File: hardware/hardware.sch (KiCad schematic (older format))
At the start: 12 parts, among them P1 CONN_01X08, P2 CONN_01X08, P3 CONN_01X02, P4 CONN_01X03

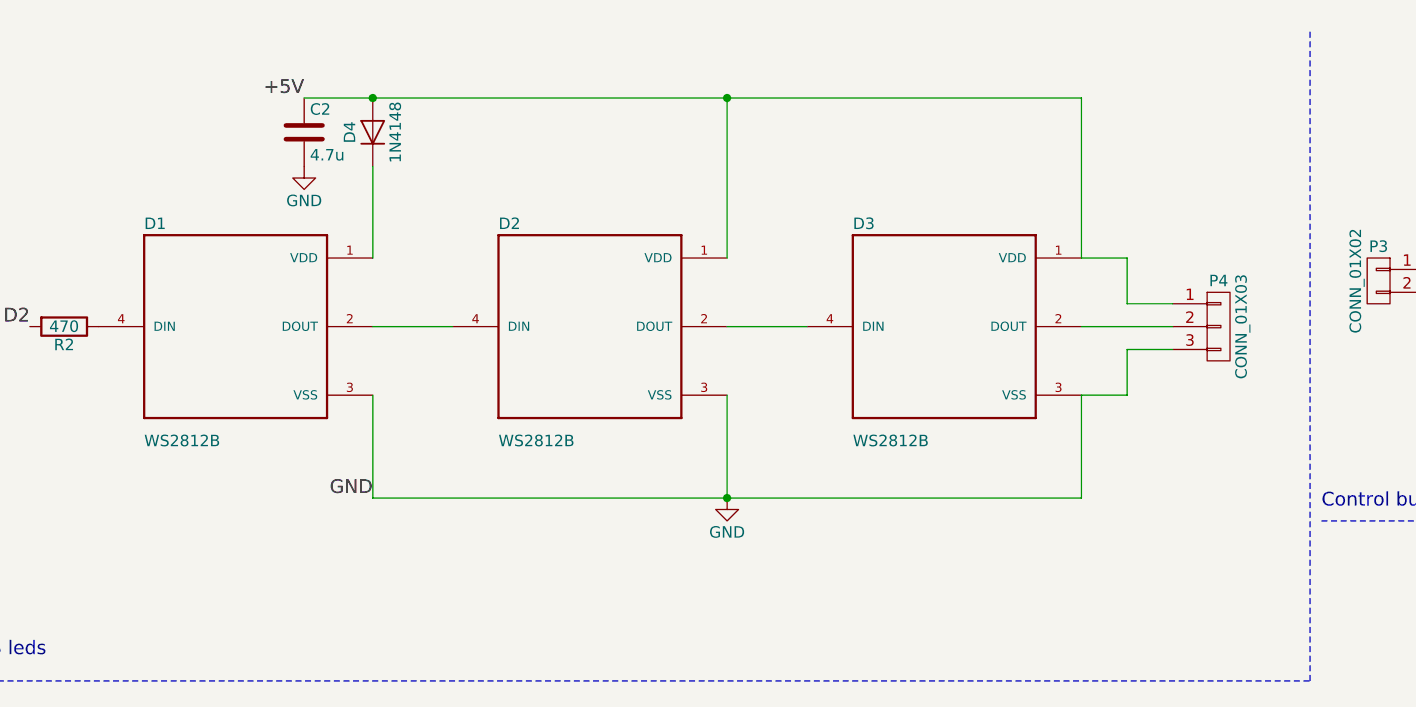
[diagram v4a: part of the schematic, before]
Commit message: v3.1, refactoring for only one Neopixel
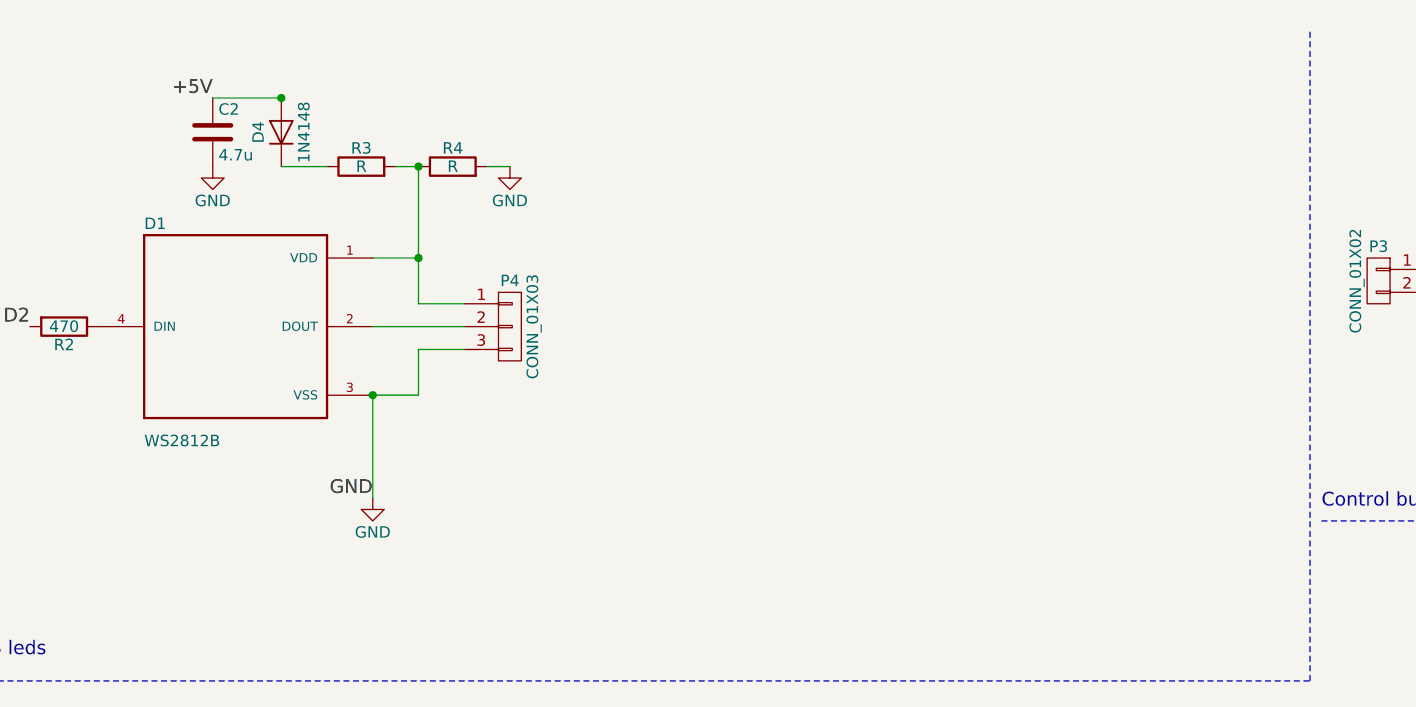
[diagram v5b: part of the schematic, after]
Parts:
- removed D2, D3: WS2812B, WS2812B:LED_WS2812B, symbol WS2812B
- added R3, R4: R, Resistors_THT:R_Axial_DIN0204_L3.6mm_D1.6mm_P2.54mm_Vertical, symbol R
- C1, C2: footprint Capacitors_SMD:C_0402 -> Capacitors_THT:C_Disc_D3.8mm_W2.6mm_P2.50mm
- D4: footprint Diodes_SMD:MiniMELF_Standard -> Diodes_THT:D_DO-15_P2.54mm_Vertical_KathodeUp
- P3: footprint Connect:PINHEAD1-2 -> Pin_Headers:Pin_Header_Angled_1x02
- P4: footprint Connect:PINHEAD1-3 -> Pin_Headers:Pin_Header_Angled_1x03
- R1, R2: footprint Resistors_SMD:R_0402 -> Resistors_THT:R_Axial_DIN0204_L3.6mm_D1.6mm_P2.54mm_Vertical
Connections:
- net +5V: no longer P4.1 (P1)
- net GND: now also R4.2
- net at D1.1 (VDD): now also P4.1 (P1), R3.2, R4.1; no longer D4.1 (K)
- net at D1.2 (DOUT): now also P4.2 (P2)
- new net: D4.1 (K), R3.1
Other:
- moved on the sheet: C2, D4, P4
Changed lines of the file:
@@
 encoding utf-8
 Sheet 1 1
-Title "SweetTime"
-Date "2016-06-27"
-Rev "2.0"
-Comp "Galilabs"
-Comment1 "Fablab Lannion"
-Comment2 "http://u.dinask.eu/trender"
+Title "Trender Led Shield"
+Date "2018-02-18"
+Rev "3.1"
+Comp "Fablab de Lannion"
+Comment1 "http://u.dinask.eu/trender"
+Comment2 "Trender project"
 Comment3 ""
 Comment4 ""
@@
 $EndComp
 $Comp
-L WS2812B D2
-U 1 1 577174D3
-P 3300 1800
-F 0 "D2" H 2900 2250 50  0000 L CNN
-F 1 "WS2812B" H 2900 1300 50  0000 L CNN
-F 2 "WS2812B:LED_WS2812B" H 3300 1800 50  0001 L CNN
-F 3 "" H 3300 1800 60  0000 C CNN
-	1    3300 1800
-	1    0    0    -1
-$EndComp
-$Comp
-L WS2812B D3
-U 1 1 57717547
-P 4850 1800
-F 0 "D3" H 4450 2250 50  0000 L CNN
-F 1 "WS2812B" H 4450 1300 50  0000 L CNN
-F 2 "WS2812B:LED_WS2812B" H 4850 1800 50  0001 L CNN
-F 3 "" H 4850 1800 60  0000 C CNN
-	1    4850 1800
-	1    0    0    -1
-$EndComp
-Wire Wire Line
-	3900 1800 4250 1800
-Wire Wire Line
-	2350 1800 2700 1800
-$Comp
 L D D4
 U 1 1 57717974
-P 2350 950
-F 0 "D4" H 2350 1050 50  0000 C CNN
-F 1 "1N4148" H 2350 850 50  0000 C CNN
-F 2 "Diodes_SMD:MiniMELF_Standard" H 2350 950 60  0001 C CNN
-F 3 "" H 2350 950 60  0000 C CNN
-	1    2350 950
+P 1950 950
+F 0 "D4" H 1950 1050 50  0000 C CNN
+F 1 "1N4148" H 1950 850 50  0000 C CNN
+F 2 "Diodes_THT:D_DO-15_P2.54mm_Vertical_KathodeUp" H 1950 950 60  0001 C CNN
+F 3 "" H 1950 950 60  0000 C CNN
+	1    1950 950
 	0    -1   -1   0
 $EndComp
 Wire Wire Line
-	2350 1500 2350 1100
-Wire Wire Line
-	2050 800  5450 800
-Wire Wire Line
-	3900 800  3900 1500
-Wire Wire Line
-	5450 800  5450 1500
-Connection ~ 3900 800
-Text Label 2050 800  2    60   ~ 0
+	1650 800  1950 800
+Text Label 1650 800  2    60   ~ 0
 +5V
 Wire Wire Line
 	2350 2100 2350 2550
-Wire Wire Line
-	2350 2550 5450 2550
-Wire Wire Line
-	3900 2550 3900 2100
-Wire Wire Line
-	5450 2550 5450 2100
-Connection ~ 3900 2550
 Text Label 2350 2550 2    60   ~ 0
 GND
@@
 F 0 "R1" V 7380 1000 50  0000 C CNN
 F 1 "10K" V 7300 1000 50  0000 C CNN
-F 2 "Resistors_SMD:R_0402" V 7230 1000 30  0001 C CNN
+F 2 "Resistors_THT:R_Axial_DIN0204_L3.6mm_D1.6mm_P2.54mm_Vertical" V 7230 1000 30  0001 C CNN
 F 3 "" H 7300 1000 30  0000 C CNN
 	1    7300 1000
@@
 F 0 "C1" H 7325 1650 50  0000 L CNN
 F 1 "10n" H 7325 1450 50  0000 L CNN
-F 2 "Capacitors_SMD:C_0402" H 7338 1400 30  0001 C CNN
+F 2 "Capacitors_THT:C_Disc_D3.8mm_W2.6mm_P2.50mm" H 7338 1400 30  0001 C CNN
 F 3 "" H 7300 1550 60  0000 C CNN
 	1    7300 1550
@@
 L GND #PWR06
 U 1 1 5771848D
-P 3900 2550
-F 0 "#PWR06" H 3900 2300 50  0001 C CNN
-F 1 "GND" H 3900 2400 50  0000 C CNN
-F 2 "" H 3900 2550 60  0000 C CNN
-F 3 "" H 3900 2550 60  0000 C CNN
-	1    3900 2550
+P 2350 2550
+F 0 "#PWR06" H 2350 2300 50  0001 C CNN
+F 1 "GND" H 2350 2400 50  0000 C CNN
+F 2 "" H 2350 2550 60  0000 C CNN
+F 3 "" H 2350 2550 60  0000 C CNN
+	1    2350 2550
 	1    0    0    -1
 $EndComp
@@
 F 0 "P3" H 6750 1750 50  0000 C CNN
 F 1 "CONN_01X02" V 6850 1600 50  0000 C CNN
-F 2 "Connect:PINHEAD1-2" H 6750 1600 60  0001 C CNN
+F 2 "Pin_Headers:Pin_Header_Angled_1x02" H 6750 1600 60  0001 C CNN
 F 3 "" H 6750 1600 60  0000 C CNN
 	1    6750 1600
@@
 F 0 "R2" V 1080 1800 50  0000 C CNN
 F 1 "470" V 1000 1800 50  0000 C CNN
-F 2 "Resistors_SMD:R_0402" V 930 1800 30  0001 C CNN
+F 2 "Resistors_THT:R_Axial_DIN0204_L3.6mm_D1.6mm_P2.54mm_Vertical" V 930 1800 30  0001 C CNN
 F 3 "" H 1000 1800 30  0000 C CNN
 	1    1000 1800
@@
 L C C2
 U 1 1 5772A7DC
-P 2050 950
-F 0 "C2" H 2075 1050 50  0000 L CNN
-F 1 "4.7u" H 2075 850 50  0000 L CNN
-F 2 "Capacitors_SMD:C_0402" H 2088 800 30  0001 C CNN
-F 3 "" H 2050 950 60  0000 C CNN
-	1    2050 950
-	1    0    0    -1
-$EndComp
-Connection ~ 2350 800
+P 1650 950
+F 0 "C2" H 1675 1050 50  0000 L CNN
+F 1 "4.7u" H 1675 850 50  0000 L CNN
+F 2 "Capacitors_THT:C_Disc_D3.8mm_W2.6mm_P2.50mm" H 1688 800 30  0001 C CNN
+F 3 "" H 1650 950 60  0000 C CNN
+	1    1650 950
+	1    0    0    -1
+$EndComp
+Connection ~ 1950 800
 $Comp
 L GND #PWR07
 U 1 1 5772A872
-P 2050 1100
-F 0 "#PWR07" H 2050 850 50  0001 C CNN
-F 1 "GND" H 2050 950 50  0000 C CNN
-F 2 "" H 2050 1100 60  0000 C CNN
-F 3 "" H 2050 1100 60  0000 C CNN
-	1    2050 1100
+P 1650 1100
+F 0 "#PWR07" H 1650 850 50  0001 C CNN
+F 1 "GND" H 1650 950 50  0000 C CNN
+F 2 "" H 1650 1100 60  0000 C CNN
+F 3 "" H 1650 1100 60  0000 C CNN
+	1    1650 1100
 	1    0    0    -1
 $EndComp
@@
 L CONN_01X03 P4
 U 1 1 5772F386
-P 6050 1800
-F 0 "P4" H 6050 2000 50  0000 C CNN
-F 1 "CONN_01X03" V 6150 1800 50  0000 C CNN
-F 2 "Connect:PINHEAD1-3" H 6050 1800 60  0001 C CNN
-F 3 "" H 6050 1800 60  0000 C CNN
-	1    6050 1800
-	1    0    0    -1
-$EndComp
-Wire Wire Line
-	5450 1500 5650 1500
-Wire Wire Line
-	5650 1500 5650 1700
-Wire Wire Line
-	5650 1700 5850 1700
-Wire Wire Line
-	5450 1800 5850 1800
-Wire Wire Line
-	5450 2100 5650 2100
-Wire Wire Line
-	5650 2100 5650 1900
-Wire Wire Line
-	5650 1900 5850 1900
+P 2950 1800
+F 0 "P4" H 2950 2000 50  0000 C CNN
+F 1 "CONN_01X03" V 3050 1800 50  0000 C CNN
+F 2 "Pin_Headers:Pin_Header_Angled_1x03" H 2950 1800 60  0001 C CNN
+F 3 "" H 2950 1800 60  0000 C CNN
+	1    2950 1800
+	1    0    0    -1
+$EndComp
+Wire Wire Line
+	2350 1500 2550 1500
+Wire Wire Line
+	2550 1100 2550 1700
+Wire Wire Line
+	2550 1700 2750 1700
+Wire Wire Line
+	2350 1800 2750 1800
+Wire Wire Line
+	2350 2100 2550 2100
+Wire Wire Line
+	2550 2100 2550 1900
+Wire Wire Line
+	2550 1900 2750 1900
+$Comp
+L R R3
+U 1 1 5A894C13
+P 2300 1100
+F 0 "R3" V 2380 1100 50  0000 C CNN
+F 1 "R" V 2300 1100 50  0000 C CNN
+F 2 "Resistors_THT:R_Axial_DIN0204_L3.6mm_D1.6mm_P2.54mm_Vertical" V 2230 1100 50  0001 C CNN
+F 3 "" H 2300 1100 50  0001 C CNN
+	1    2300 1100
+	0    -1   -1   0
+$EndComp
+$Comp
+L R R4
+U 1 1 5A894D26
+P 2700 1100
+F 0 "R4" V 2780 1100 50  0000 C CNN
+F 1 "R" V 2700 1100 50  0000 C CNN
+F 2 "Resistors_THT:R_Axial_DIN0204_L3.6mm_D1.6mm_P2.54mm_Vertical" V 2630 1100 50  0001 C CNN
+F 3 "" H 2700 1100 50  0001 C CNN
+	1    2700 1100
+	0    -1   -1   0
+$EndComp
+$Comp
+L GND #PWR08
+U 1 1 5A894DFE
+P 2950 1100
+F 0 "#PWR08" H 2950 850 50  0001 C CNN
+F 1 "GND" H 2950 950 50  0000 C CNN
+F 2 "" H 2950 1100 50  0001 C CNN
+F 3 "" H 2950 1100 50  0001 C CNN
+	1    2950 1100
+	1    0    0    -1
+$EndComp
+Wire Wire Line
+	1950 1100 2150 1100
+Wire Wire Line
+	2450 1100 2550 1100
+Wire Wire Line
+	2850 1100 2950 1100
+Connection ~ 2550 1500
+Connection ~ 2550 1100
+Connection ~ 2350 2100
 $EndSCHEMATC
